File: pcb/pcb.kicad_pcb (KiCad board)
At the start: 2 copper layers, 99.9 x 87 mm, 128 parts, among them SW1 SW_Push, SW2 SW_Push, SW3 SW_Push

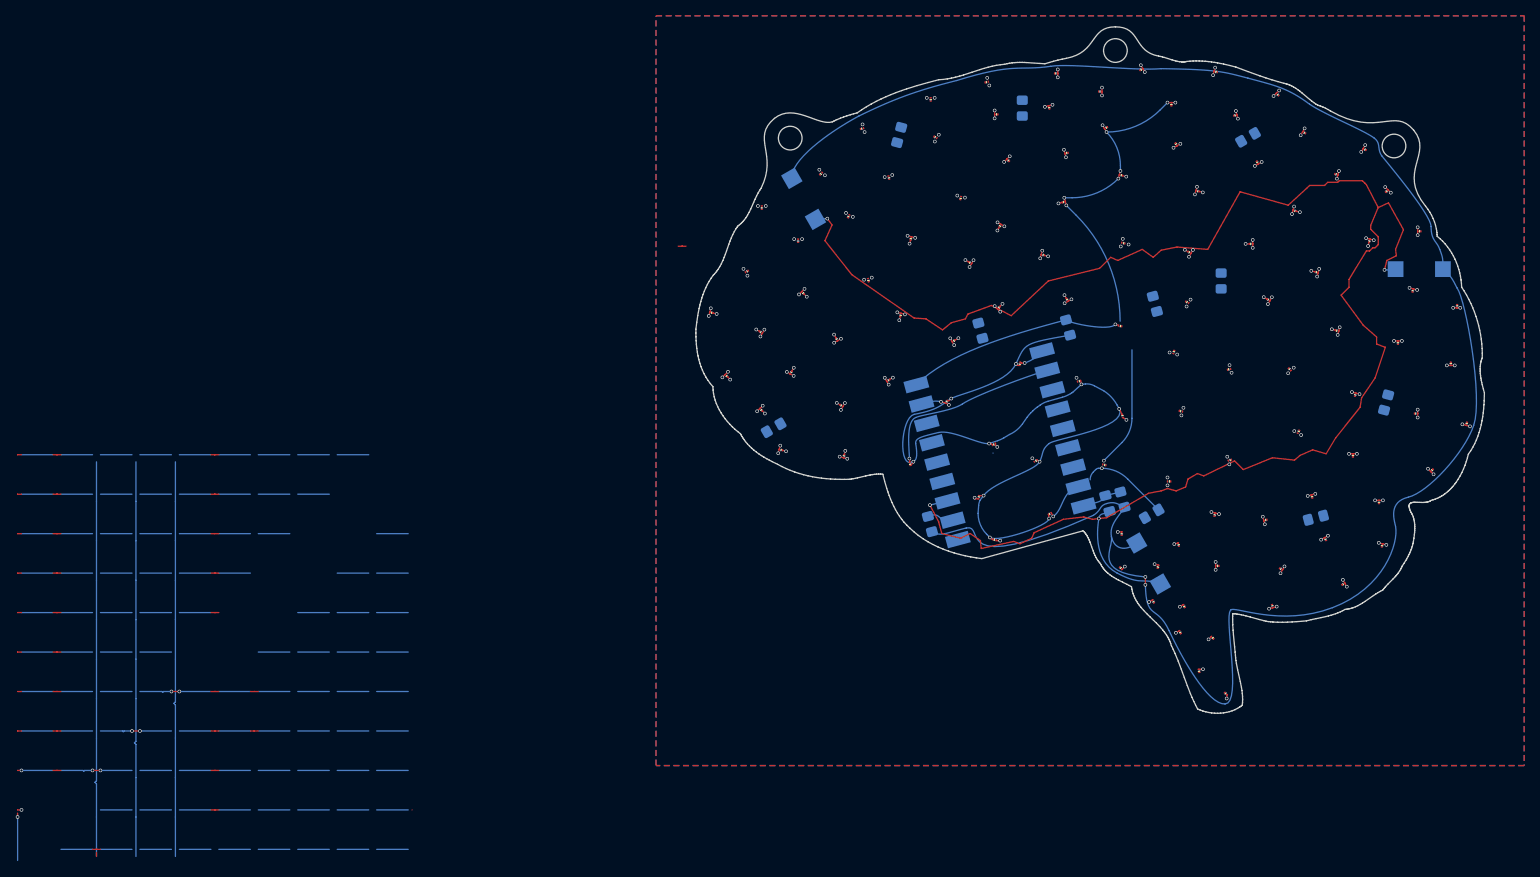
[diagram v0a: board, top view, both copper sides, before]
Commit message: routed Col0 with curves
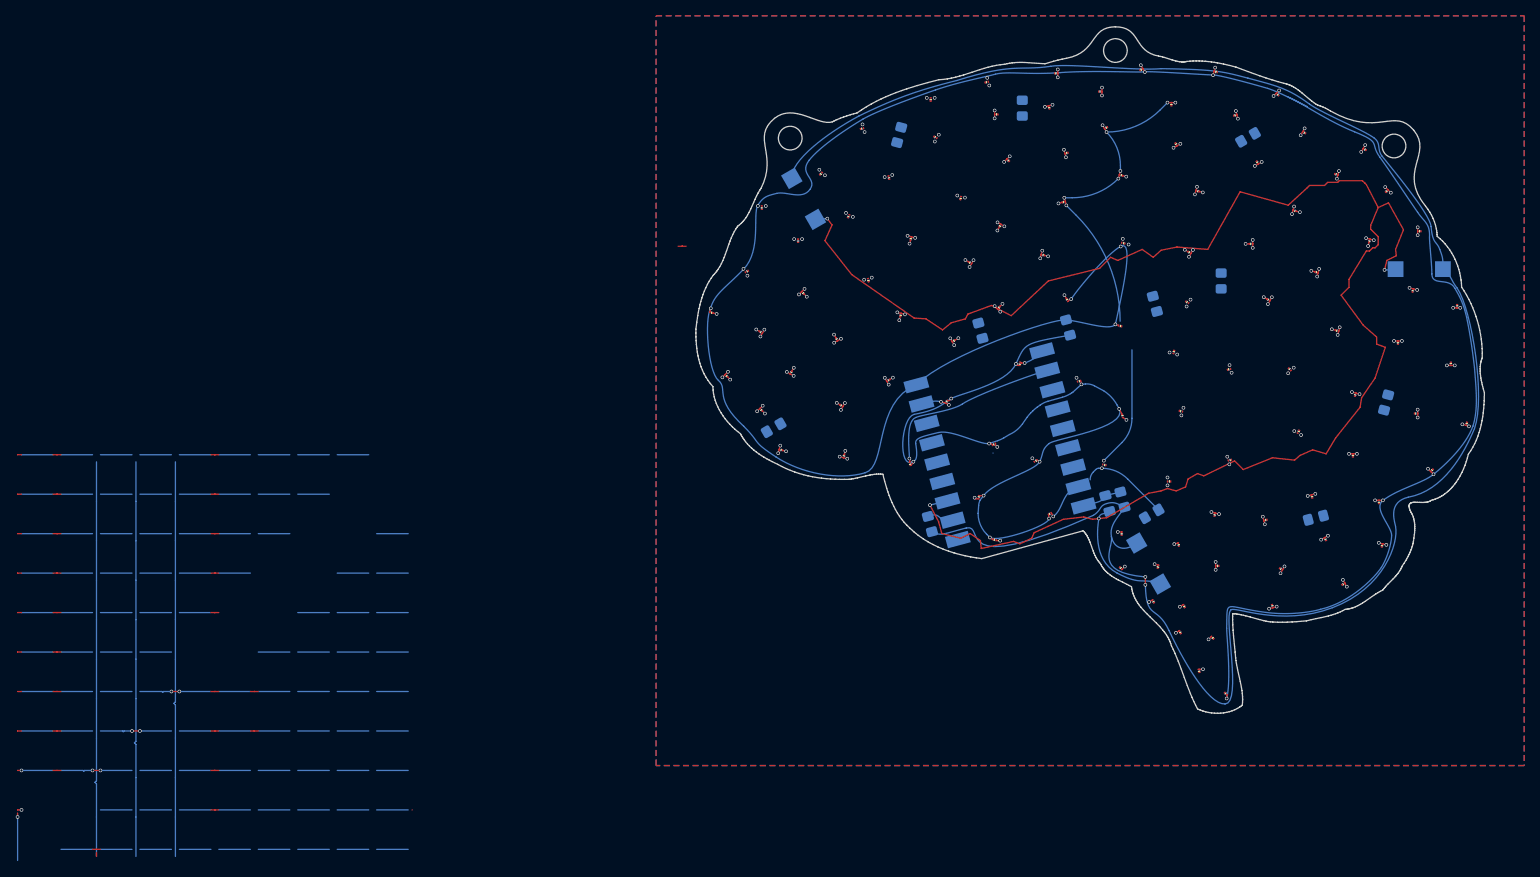
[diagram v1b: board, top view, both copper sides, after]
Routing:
- net /Col0: track 44.9 -> 44.0 mm
- net /Col3: vias 20 -> 19
- net /Col2: vias 22 -> 21

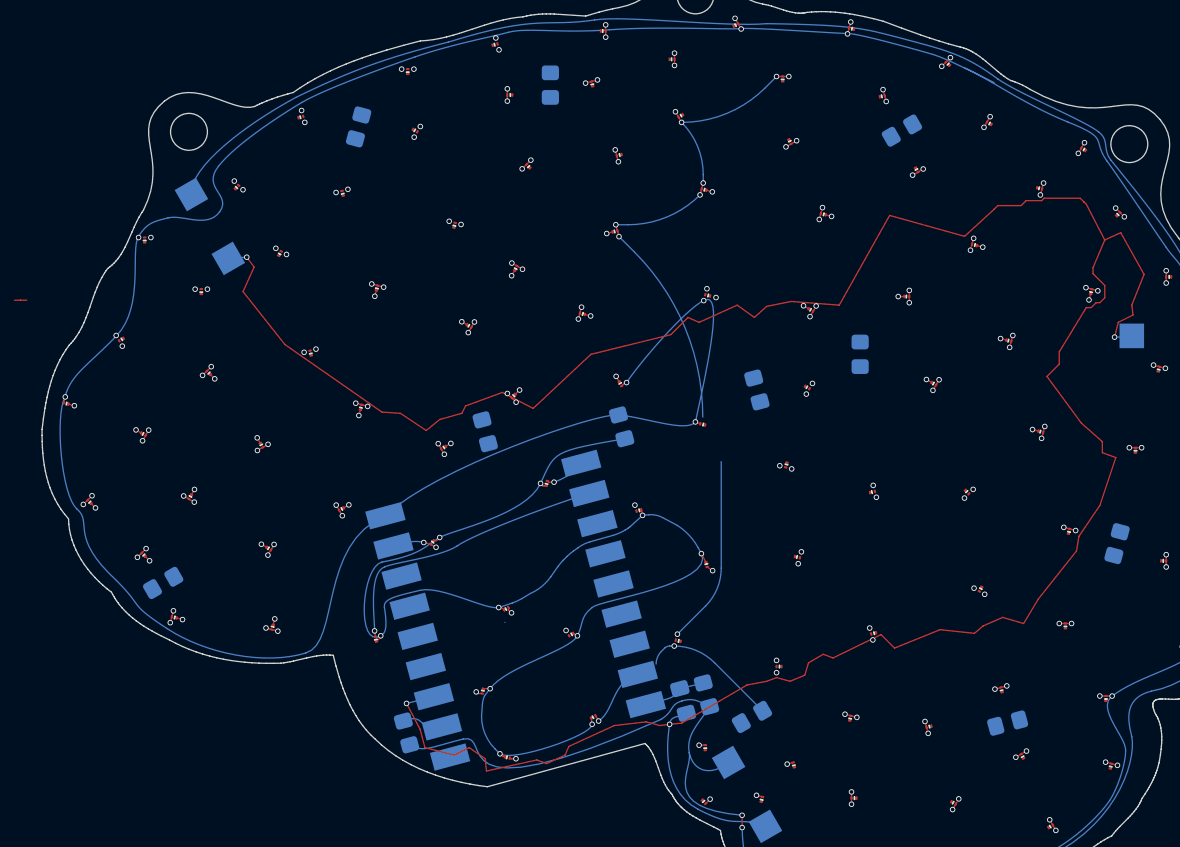
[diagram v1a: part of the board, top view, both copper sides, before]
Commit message: routed Row1, Row4 and Col10
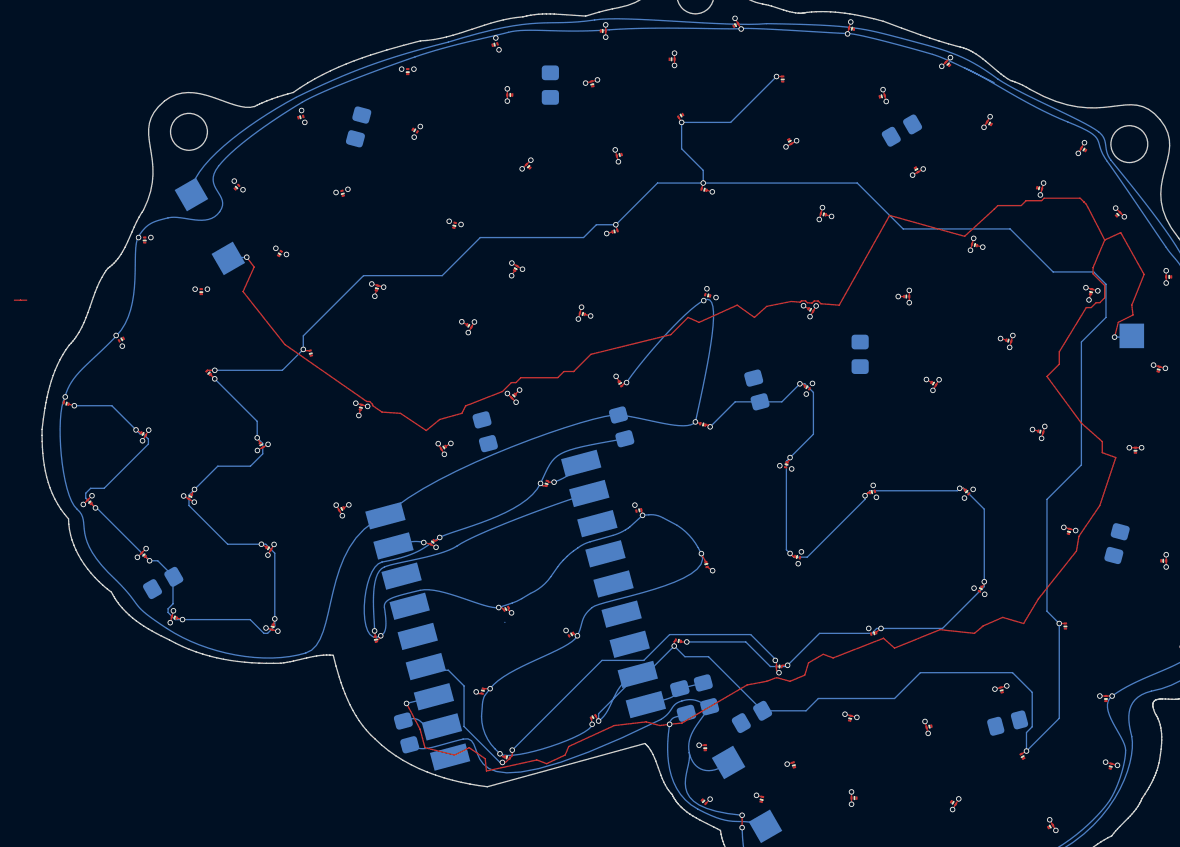
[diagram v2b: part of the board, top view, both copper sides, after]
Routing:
- net /Col10: track 111.1 -> 230.4 mm, vias 19 -> 10
- net /Row1: track 0.00 -> 82.5 mm, vias 0 -> 10
- net /Row4: track 55.1 -> 122.8 mm
- net /Col9: track 41.6 -> 81.3 mm, vias 18 -> 19
- net +3V3: track 202.7 -> 202.0 mm, vias 5 -> 4

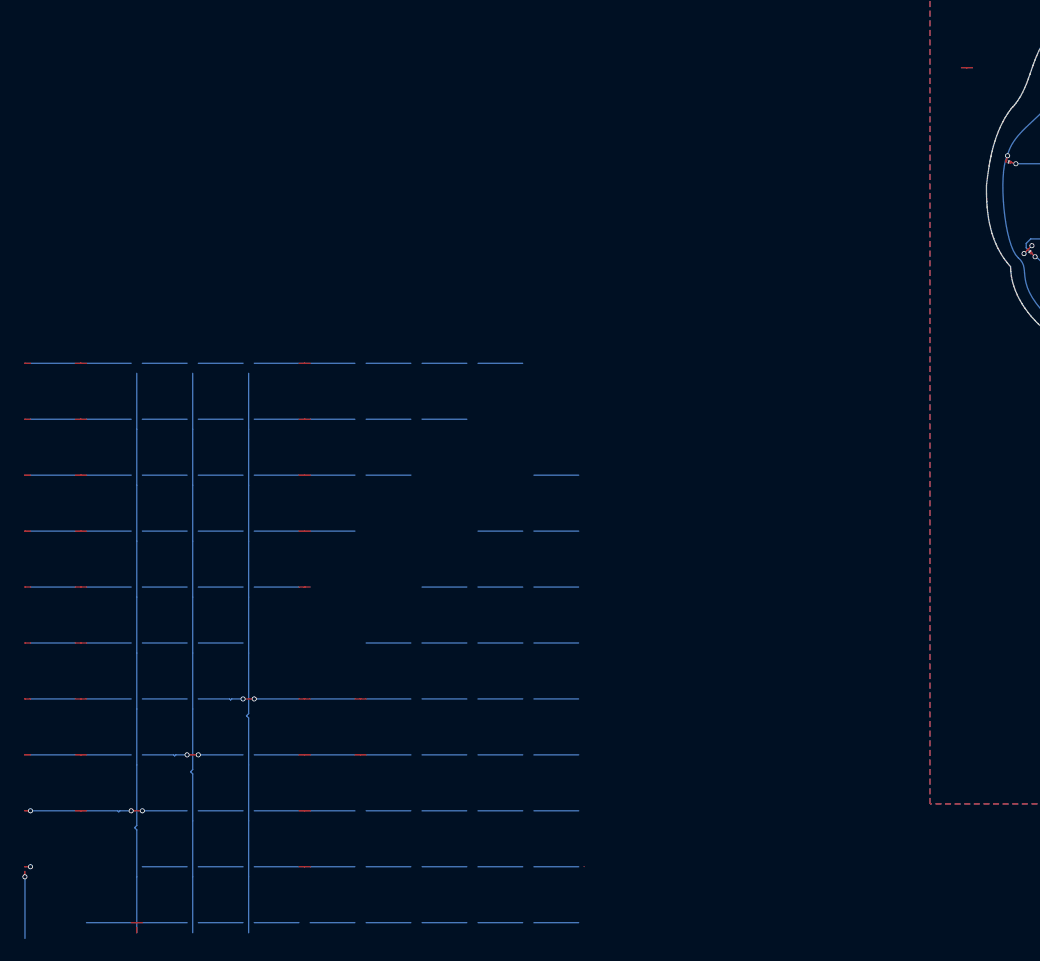
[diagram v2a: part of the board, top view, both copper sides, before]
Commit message: deleted obsolete tracks
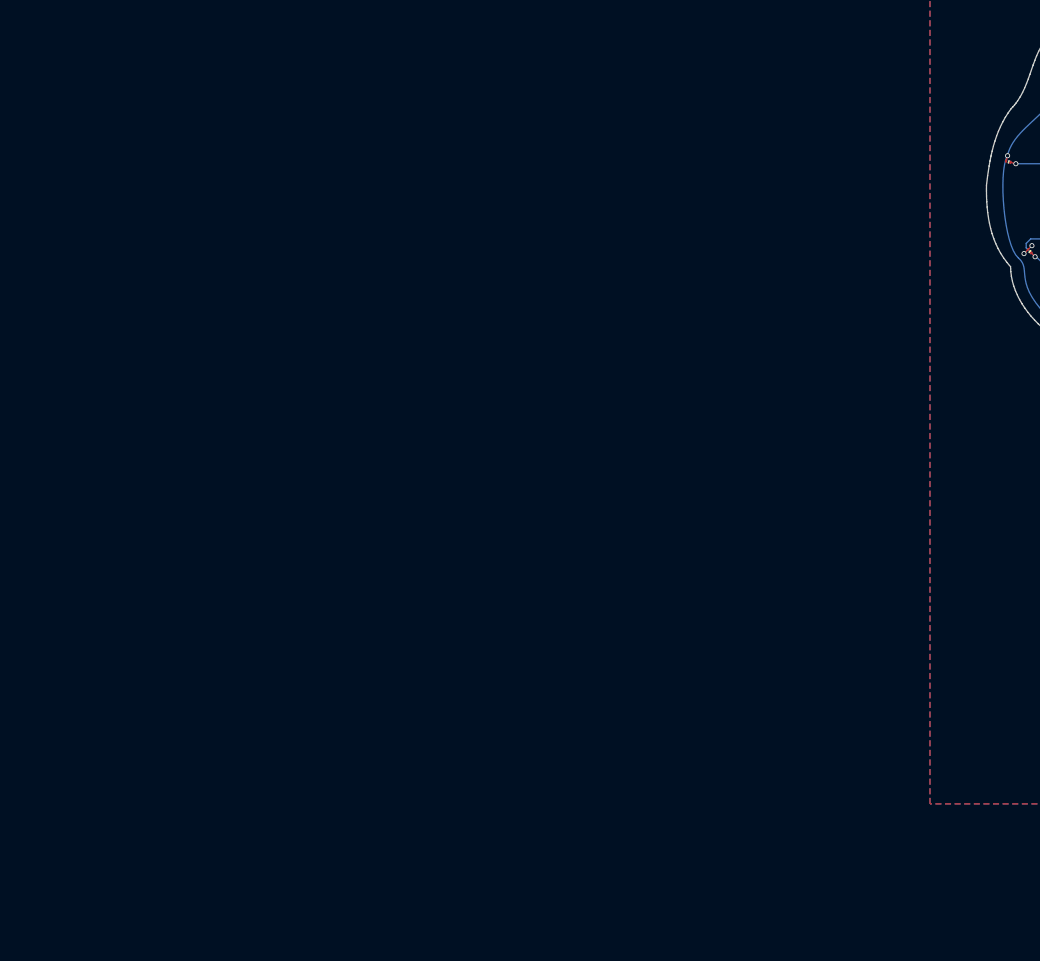
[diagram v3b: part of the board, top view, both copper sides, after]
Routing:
- net /Row2: track 55.1 -> 4.45 mm
- net /Row3: track 55.1 -> 4.95 mm
- net /Row4: track 122.8 -> 72.7 mm
- net /Col3: track 50.5 -> 5.92 mm, vias 19 -> 17
- net /Col4: track 50.7 -> 6.06 mm, vias 20 -> 18
- net /Col2: track 51.2 -> 7.61 mm, vias 21 -> 18
- net /Col10: track 230.4 -> 191.8 mm
- net /Col0: track 44.0 -> 5.94 mm
- net /Col7: track 41.0 -> 6.53 mm
- net /Col9: track 81.3 -> 46.7 mm
- net /Col8: track 41.6 -> 7.06 mm
- net /Col6: track 41.6 -> 7.07 mm
- net /Col1: track 41.7 -> 8.23 mm, vias 19 -> 18
- net /Col5: track 41.0 -> 7.53 mm
- net /Row0: track 37.6 -> 31.5 mm, vias 11 -> 10

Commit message: routed Row2, Row3 and Row5
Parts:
- turned D106 to -75 degrees
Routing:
- net /Row2: track 4.45 -> 96.8 mm
- net /Row5: track 0.00 -> 91.5 mm, vias 0 -> 10
- net /Row3: track 4.95 -> 84.7 mm
- net /Col10: track 191.8 -> 192.4 mm
